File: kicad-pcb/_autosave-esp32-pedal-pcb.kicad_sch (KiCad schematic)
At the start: 52 parts, among them J1 USB_C_Receptacle_USB2.0_14P, SW1 SW_SPST, SW2 SW_SPST, U1 MCP73871, U2 TLV75733PDBV, U3 ESP32-S3-WROOM-1, U4 TPD2EUSB30, U6 TPS2553DBVR

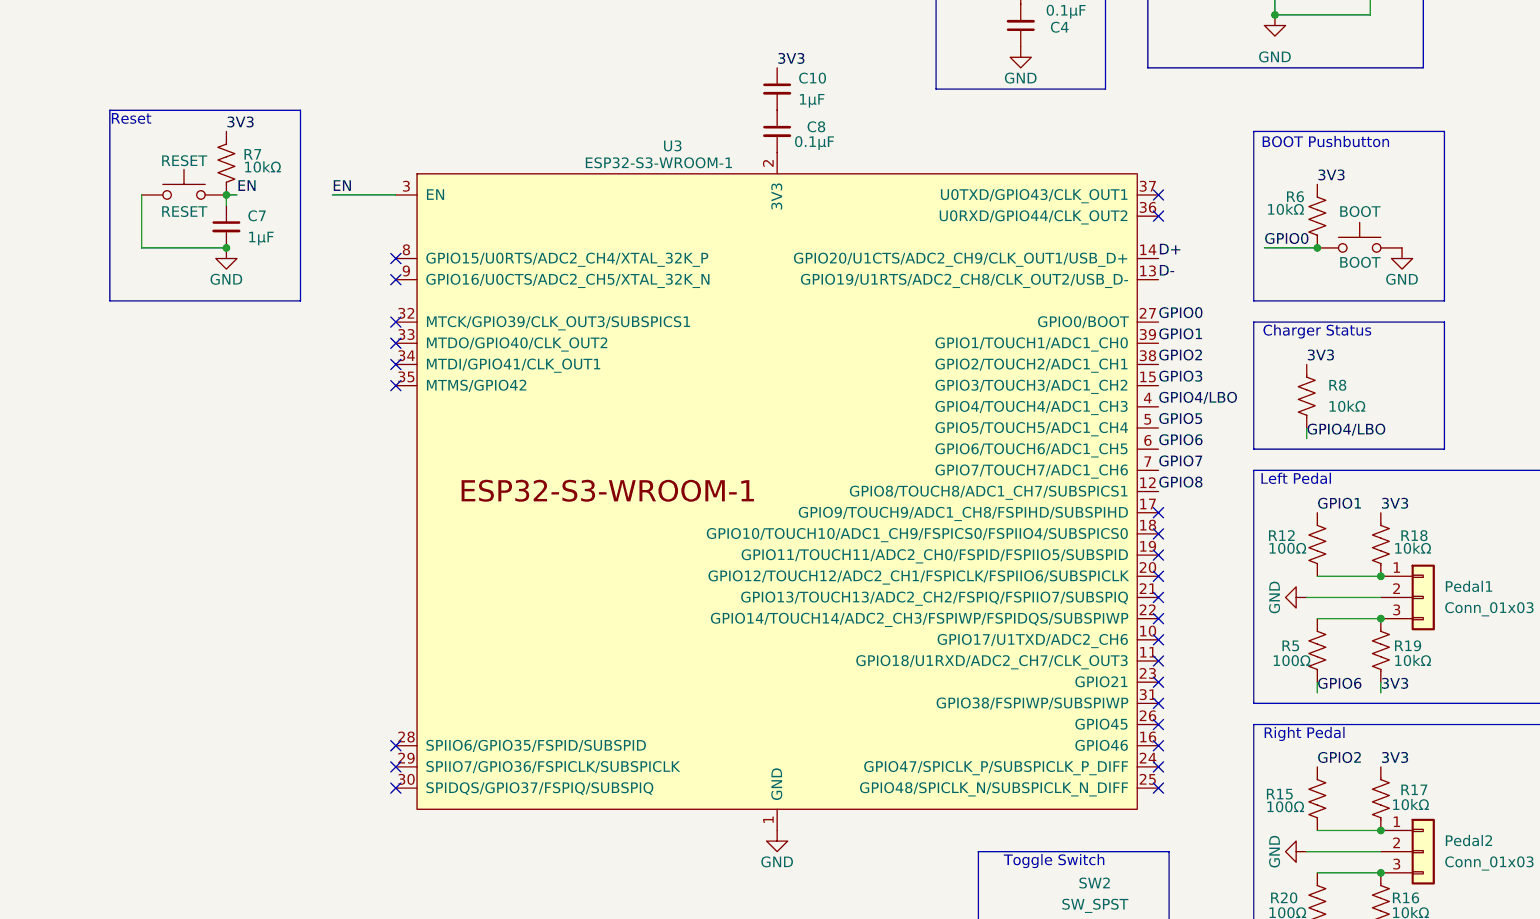
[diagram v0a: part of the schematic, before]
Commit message: Remove zip files and update PCB files
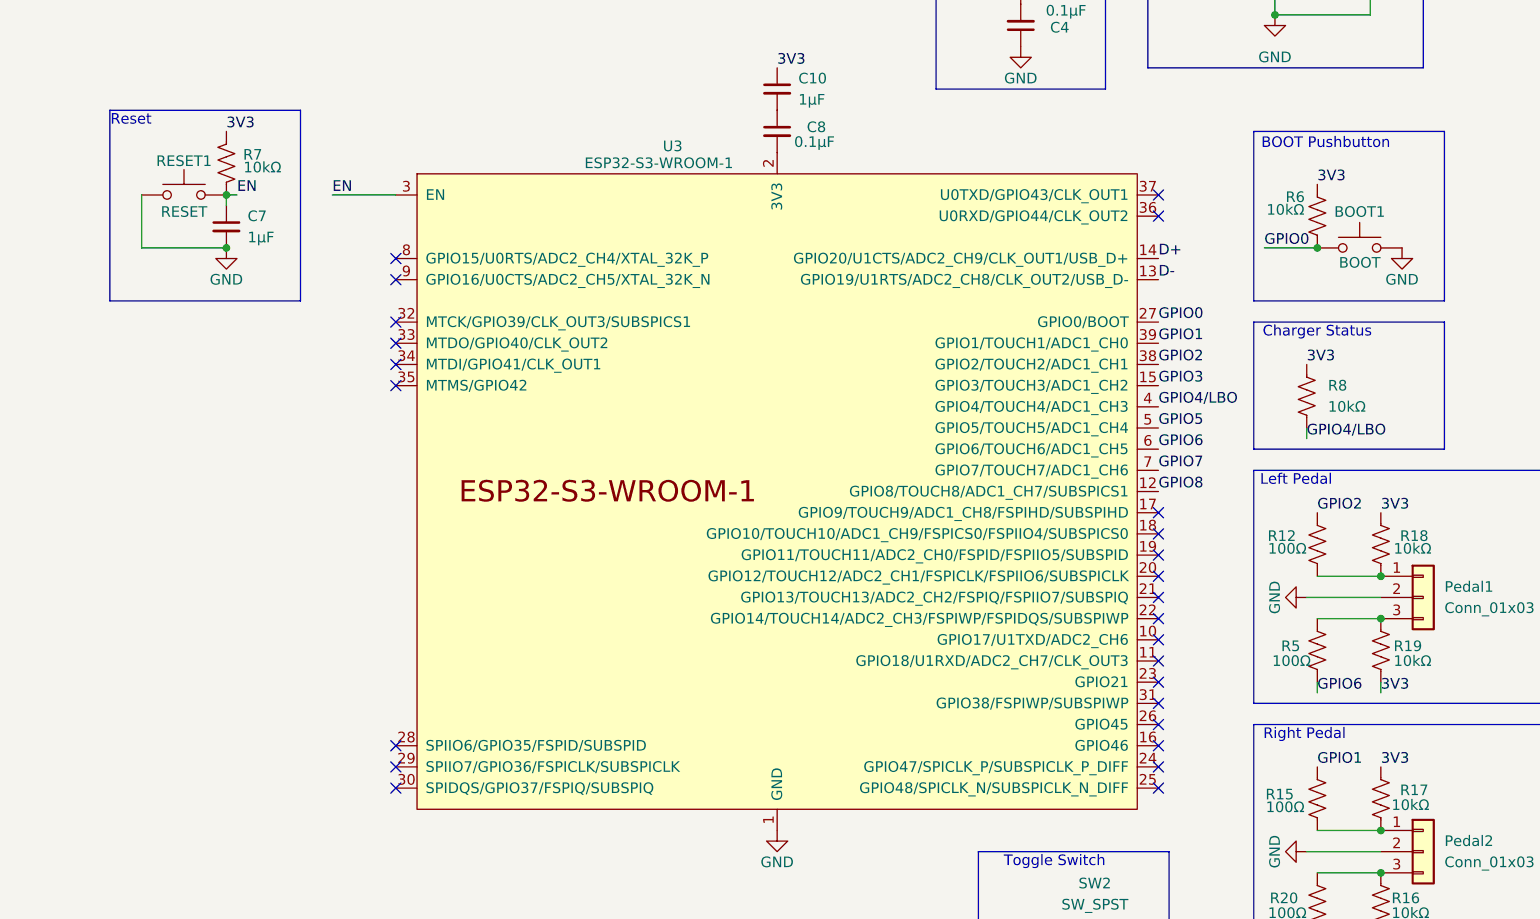
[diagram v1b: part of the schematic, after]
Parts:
- renumbered BOOT to BOOT1, RESET to RESET1
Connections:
- net GPIO1: now also R15.2; no longer R12.2
- net GPIO2: now also R12.2; no longer R15.2
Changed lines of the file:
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@@
 		)
 	)
-	(label "GPIO2"
+	(label "GPIO1"
 		(at 175.26 236.22 0)
 		(effects
@@
 		)
 	)
-	(label "GPIO1"
+	(label "GPIO2"
 		(at 175.26 205.74 0)
 		(effects
@@
 		(on_board yes)
 		(dnp no)
-		(property "Reference" "BOOT"
+		(property "Reference" "BOOT1"
 			(at 180.34 169.672 0)
 			(effects
@@
 			(project "esp32-pedal-pcb"
 				(path "/5d5a7a5a-7a5a-4a5a-8a5a-5a5a5a5a5a5a"
-					(reference "BOOT")
+					(reference "BOOT1")
 					(unit 1)
 				)
@@
 		(on_board yes)
 		(dnp no)
-		(property "Reference" "RESET"
+		(property "Reference" "RESET1"
 			(at 39.37 163.576 0)
+			(do_not_autoplace yes)
 			(effects
 				(font
@@
 			(project "esp32-pedal-pcb"
 				(path "/5d5a7a5a-7a5a-4a5a-8a5a-5a5a5a5a5a5a"
-					(reference "RESET")
+					(reference "RESET1")
 					(unit 1)
 				)
